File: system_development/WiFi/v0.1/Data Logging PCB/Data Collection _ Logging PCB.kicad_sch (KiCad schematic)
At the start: 8 parts, among them U1 TC2014-3.3VxCTTR

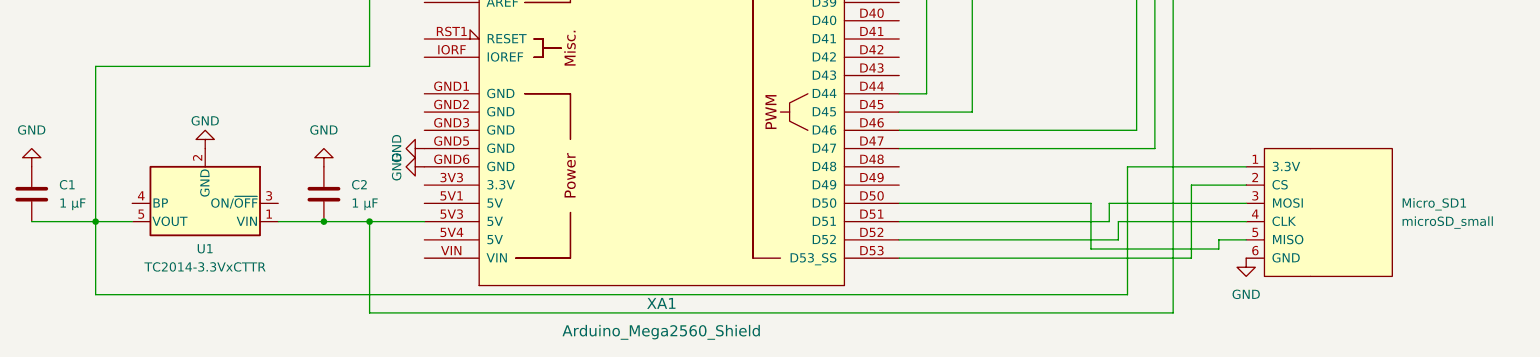
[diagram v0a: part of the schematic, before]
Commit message: Redid PCB's for Wifi Version
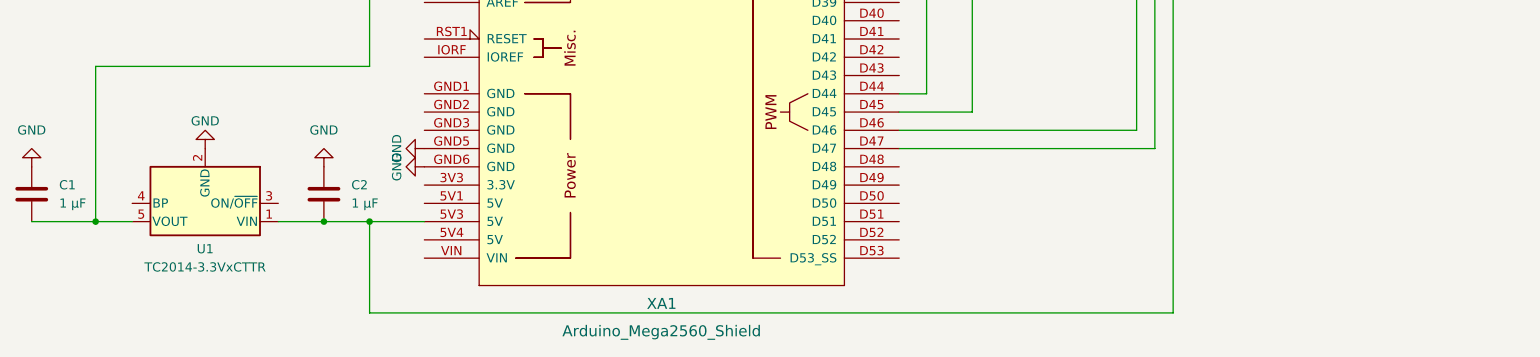
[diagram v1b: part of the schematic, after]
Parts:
- removed Micro_SD1: microSD_small, Connector_PinSocket_2.54mm:PinSocket_1x06_P2.54mm_Vertical, symbol ARTS-Lab:microSD_small
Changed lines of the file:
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@@
-    (stroke (width 0) (type default))
-  )
-  (wire (pts (xy 196.85 142.24) (xy 196.85 148.59))
     (stroke (width 0) (type default))
   )
@@
     (stroke (width 0) (type default))
   )
-  (wire (pts (xy 170.18 147.32) (xy 200.66 147.32))
-    (stroke (width 0) (type default))
-  )
   (wire (pts (xy 203.2 132.08) (xy 170.18 132.08))
     (stroke (width 0) (type default))
@@
     (stroke (width 0) (type default))
   )
-  (wire (pts (xy 199.39 142.24) (xy 218.44 142.24))
-    (stroke (width 0) (type default))
-  )
   (wire (pts (xy 227.33 99.06) (xy 203.2 99.06))
     (stroke (width 0) (type default))
   )
-  (wire (pts (xy 214.63 148.59) (xy 214.63 147.32))
-    (stroke (width 0) (type default))
-  )
   (wire (pts (xy 213.36 95.25) (xy 218.44 95.25))
     (stroke (width 0) (type default))
@@
     (stroke (width 0) (type default))
   )
-  (wire (pts (xy 196.85 148.59) (xy 214.63 148.59))
-    (stroke (width 0) (type default))
-  )
-  (wire (pts (xy 214.63 147.32) (xy 218.44 147.32))
-    (stroke (width 0) (type default))
-  )
-  (wire (pts (xy 170.18 149.86) (xy 210.82 149.86))
-    (stroke (width 0) (type default))
-  )
   (wire (pts (xy 72.39 78.74) (xy 72.39 82.55))
     (stroke (width 0) (type default))
   )
-  (wire (pts (xy 210.82 149.86) (xy 210.82 139.7))
-    (stroke (width 0) (type default))
-  )
   (wire (pts (xy 205.74 102.87) (xy 205.74 134.62))
     (stroke (width 0) (type default))
@@
     (stroke (width 0) (type default))
   )
-  (wire (pts (xy 201.93 154.94) (xy 58.42 154.94))
-    (stroke (width 0) (type default))
-  )
   (wire (pts (xy 208.28 106.68) (xy 227.33 106.68))
     (stroke (width 0) (type default))
@@
     (stroke (width 0) (type default))
   )
-  (wire (pts (xy 170.18 142.24) (xy 196.85 142.24))
-    (stroke (width 0) (type default))
-  )
-  (wire (pts (xy 170.18 144.78) (xy 199.39 144.78))
-    (stroke (width 0) (type default))
-  )
   (wire (pts (xy 208.28 157.48) (xy 208.28 106.68))
     (stroke (width 0) (type default))
@@
     (stroke (width 0) (type default))
   )
-  (wire (pts (xy 199.39 144.78) (xy 199.39 142.24))
-    (stroke (width 0) (type default))
-  )
   (wire (pts (xy 218.44 95.25) (xy 227.33 95.25))
     (stroke (width 0) (type default))
@@
     (stroke (width 0) (type default))
   )
-  (wire (pts (xy 210.82 139.7) (xy 218.44 139.7))
-    (stroke (width 0) (type default))
-  )
-  (wire (pts (xy 218.44 137.16) (xy 201.93 137.16))
-    (stroke (width 0) (type default))
-  )
   (wire (pts (xy 96.52 157.48) (xy 208.28 157.48))
     (stroke (width 0) (type default))
   )
-  (wire (pts (xy 58.42 144.78) (xy 58.42 154.94))
-    (stroke (width 0) (type default))
-  )
   (wire (pts (xy 49.53 144.78) (xy 58.42 144.78))
     (stroke (width 0) (type default))
@@
     (stroke (width 0) (type default))
   )
-  (wire (pts (xy 200.66 147.32) (xy 200.66 144.78))
-    (stroke (width 0) (type default))
-  )
   (wire (pts (xy 227.33 80.01) (xy 173.99 80.01))
-    (stroke (width 0) (type default))
-  )
-  (wire (pts (xy 201.93 137.16) (xy 201.93 154.94))
-    (stroke (width 0) (type default))
-  )
-  (wire (pts (xy 200.66 144.78) (xy 218.44 144.78))
     (stroke (width 0) (type default))
   )
@@
         (path "/0fbf51aa-9f7e-4b3e-beb6-3112974e4ac2"
           (reference "#PWR02") (unit 1)
-        )
-      )
-    )
-  )
-  (symbol (lib_id "power:GND") (at 218.44 149.86 0) (unit 1)
-    (in_bom yes) (on_board yes) (dnp no) (fields_autoplaced)
-    (property "Reference" "#PWR010" (at 218.44 156.21 0)
-      (effects (font (size 1.27 1.27)) hide)
-    )
-    (property "Value" "GND" (at 218.44 154.94 0)
-      (effects (font (size 1.27 1.27)))
-    )
-    (property "Footprint" "" (at 218.44 149.86 0)
-      (effects (font (size 1.27 1.27)) hide)
-    )
-    (property "Datasheet" "" (at 218.44 149.86 0)
-      (effects (font (size 1.27 1.27)) hide)
-    )
-    (pin "1")
-    (instances
-      (project "Data Collection _ Logging PCB"
-        (path "/0fbf51aa-9f7e-4b3e-beb6-3112974e4ac2"
-          (reference "#PWR010") (unit 1)
         )
       )
@@
         )
       )
-    )
-  )
-  (symbol (lib_id "ARTS-Lab:microSD_small") (at 238.76 143.51 270) (unit 1)
-    (in_bom yes) (on_board yes) (dnp no) (fields_autoplaced)
-    (property "Reference" "Micro_SD1" (at 240.03 142.2399 90)
-      (effects (font (size 1.27 1.27)) (justify left))
-    )
-    (property "Value" "microSD_small" (at 240.03 144.7799 90)
-      (effects (font (size 1.27 1.27)) (justify left))
-    )
-    (property "Footprint" "Connector_PinSocket_2.54mm:PinSocket_1x06_P2.54mm_Vertical" (at 238.76 143.51 0)
-      (effects (font (size 1.27 1.27)) hide)
-    )
-    (property "Datasheet" "" (at 238.76 143.51 0)
-      (effects (font (size 1.27 1.27)) hide)
-    )
-    (pin "1")
-    (pin "2")
-    (pin "3")
-    (pin "4")
-    (pin "5")
-    (pin "6")
-    (instances
-      (project "Data Collection _ Logging PCB"
-        (path "/0fbf51aa-9f7e-4b3e-beb6-3112974e4ac2"
-          (reference "Micro_SD1") (unit 1)
-        )
-      )
